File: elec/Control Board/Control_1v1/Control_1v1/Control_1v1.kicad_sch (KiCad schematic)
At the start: 104 parts, among them J1 DB9_Female_MountingHoles, J10 Conn_02x12_Odd_Even, J11 Screw_Terminal_01x02, J14 Conn_01x10, J2 Conn_01x08, J25 Screw_Terminal_01x02, J26 Conn_01x10, J27 Conn_02x12_Odd_Even, J28 Screw_Terminal_01x02, J29 Conn_01x10, J3 Conn_01x08, J4 Conn_01x08, J5 Conn_01x08, J6 Conn_01x08, J7 Conn_01x10, J8 Conn_02x18_Odd_Even, J9 Conn_01x10

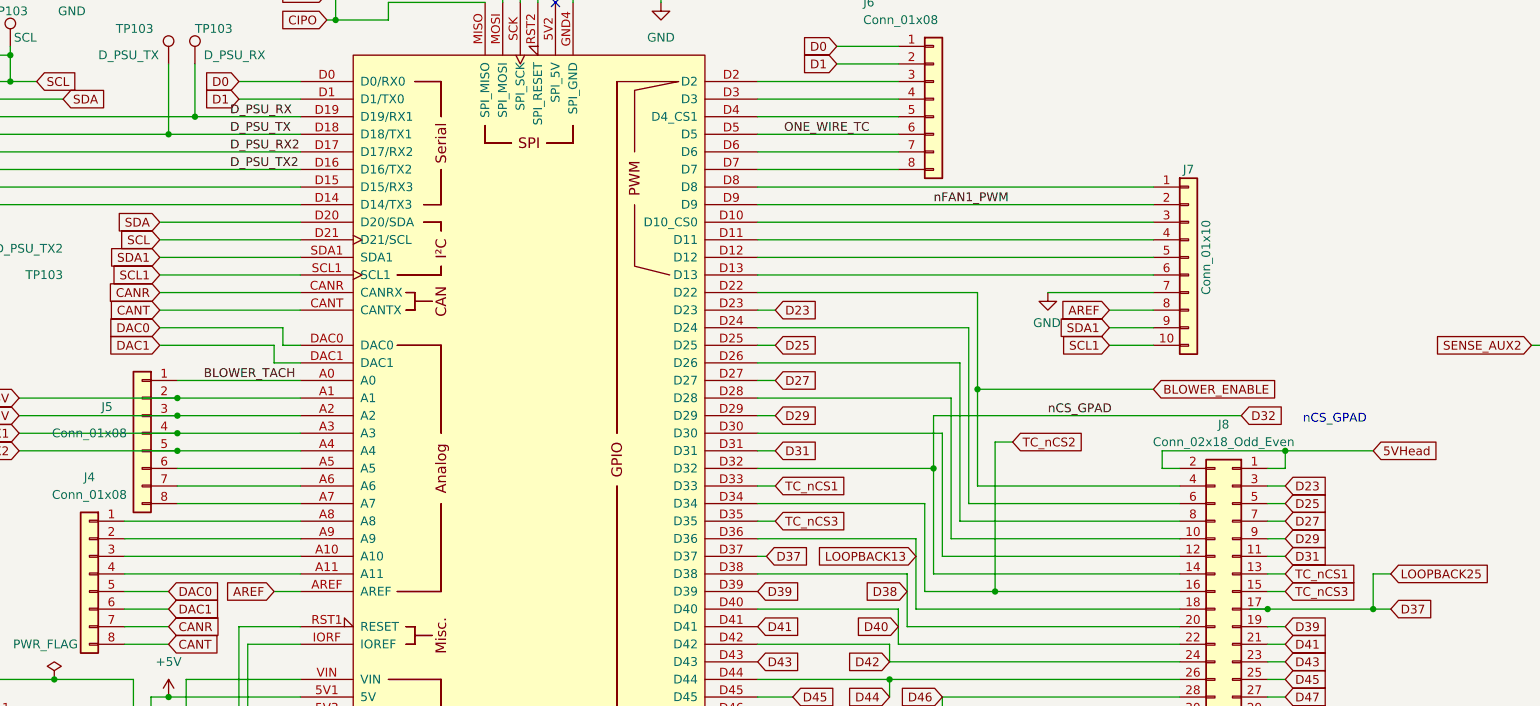
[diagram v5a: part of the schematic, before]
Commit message: Add LED_BUILTIN
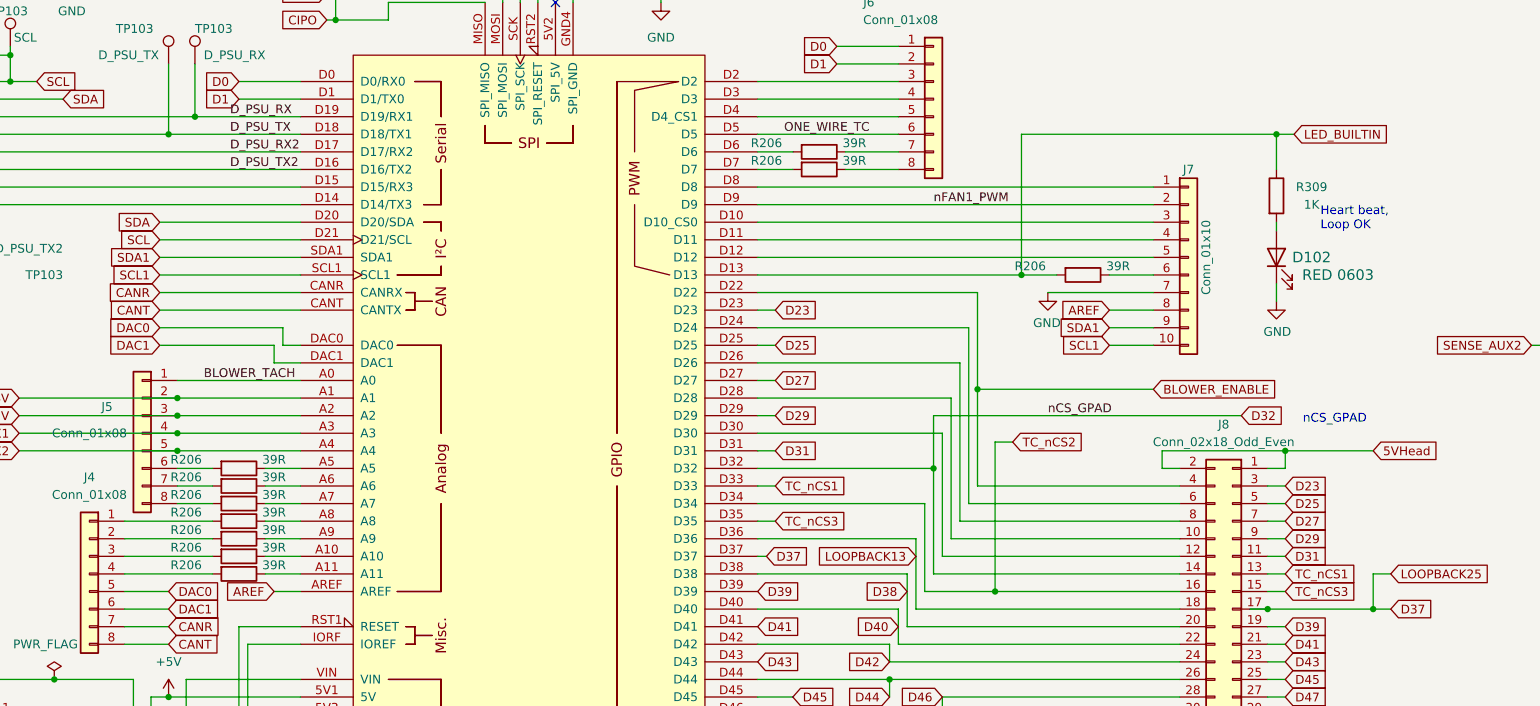
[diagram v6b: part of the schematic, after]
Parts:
- added D102: RED 0603, LED_SMD:LED_0603_1608Metric_Pad1.05x0.95mm_HandSolder, symbol Device:LED
- added R206 (x10): 39R, Resistor_SMD:R_0603_1608Metric_Pad0.98x0.95mm_HandSolder, symbol Device:R
- added R309: 1K, Resistor_SMD:R_0603_1608Metric_Pad0.98x0.95mm_HandSolder, symbol Device:R
- A1: footprint Arduino:Arduino_Due_Shield -> PubInv_KiCad_PCB:Arduino_Due_Shield_Annotated
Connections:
- net GND: now also D102.1 (K)
- net at A1.A10: now also R206.1; no longer J4.3 (Pin_3)
- net at A1.A11: now also R206.1; no longer J4.4 (Pin_4)
- net at A1.A5: now also R206.1; no longer J5.6 (Pin_6)
- net at A1.A6: now also R206.1; no longer J5.7 (Pin_7)
- net at A1.A7: now also R206.1; no longer J5.8 (Pin_8)
- net at A1.A8: now also R206.1; no longer J4.1 (Pin_1)
- net at A1.A9: now also R206.1; no longer J4.2 (Pin_2)
- net at J7.6 (Pin_6): now also R206.1; no longer A1.D13
- net at A1.D6: now also R206.2; no longer J6.7 (Pin_7)
- net at J6.8 (Pin_8): now also R206.1; no longer A1.D7
- new net: A1.D7, R206.2
- new net: D102.2 (A), R309.2
- new net: J4.1 (Pin_1), R206.2
- new net: J4.2 (Pin_2), R206.2
- new net: J4.3 (Pin_3), R206.2
- new net: J4.4 (Pin_4), R206.2
- new net: J5.7 (Pin_7), R206.2
- new net: J5.6 (Pin_6), R206.2
- new net: J5.8 (Pin_8), R206.2
- new net: J6.7 (Pin_7), R206.1
- new net LED_BUILTIN: A1.D13, R206.2, R309.1
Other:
- note added: "Heart beat, Loop OK"

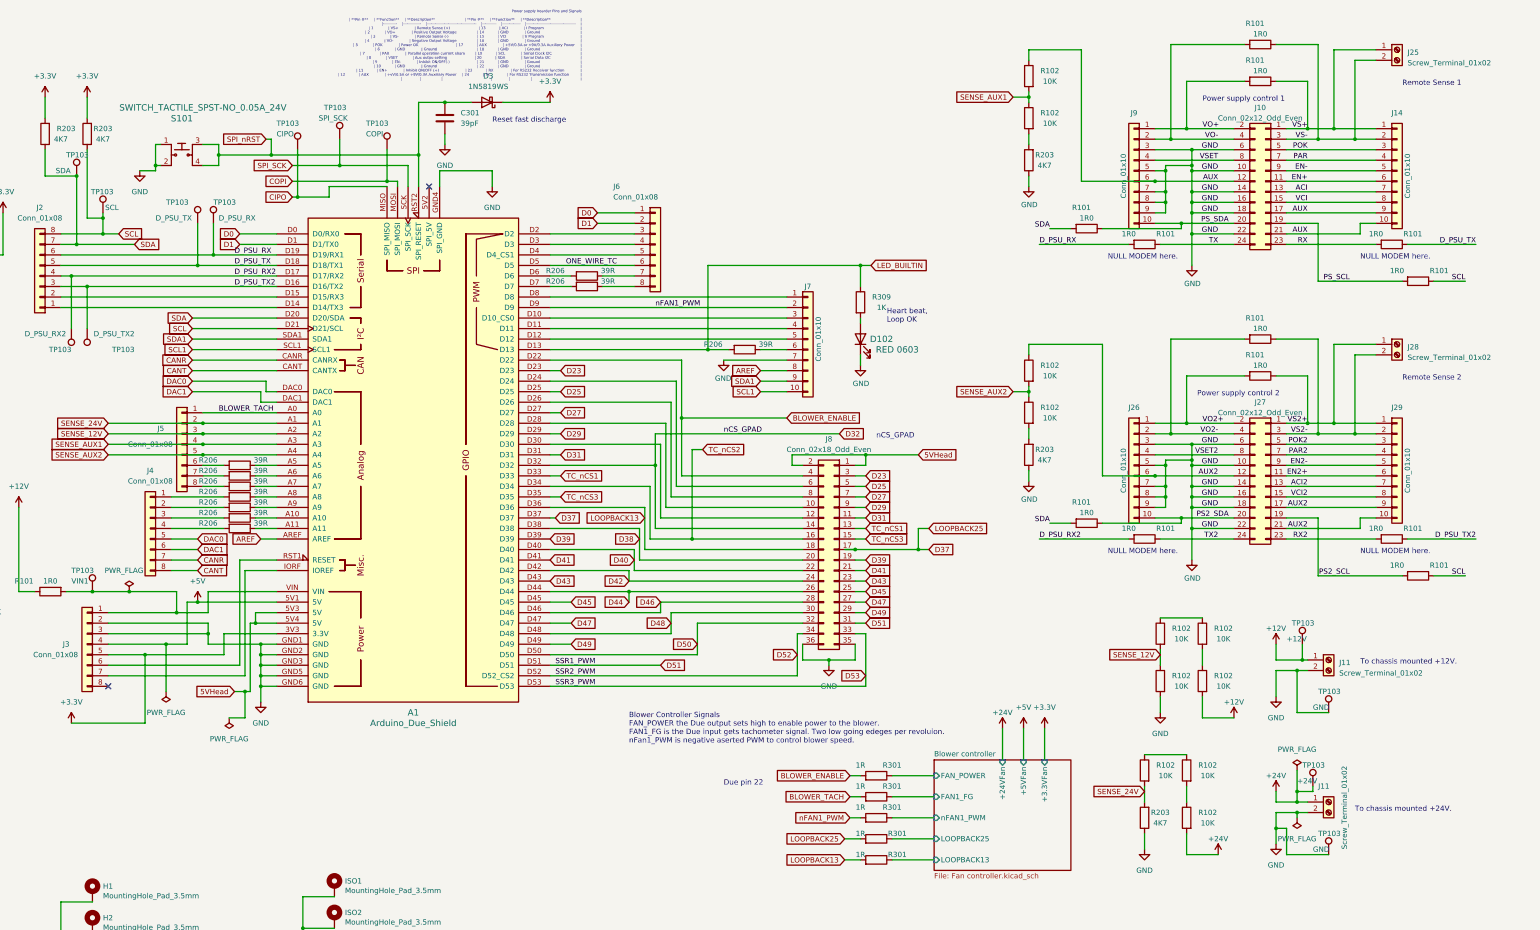
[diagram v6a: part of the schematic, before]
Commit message: Add power supply enable circuits. Add shutdown button.
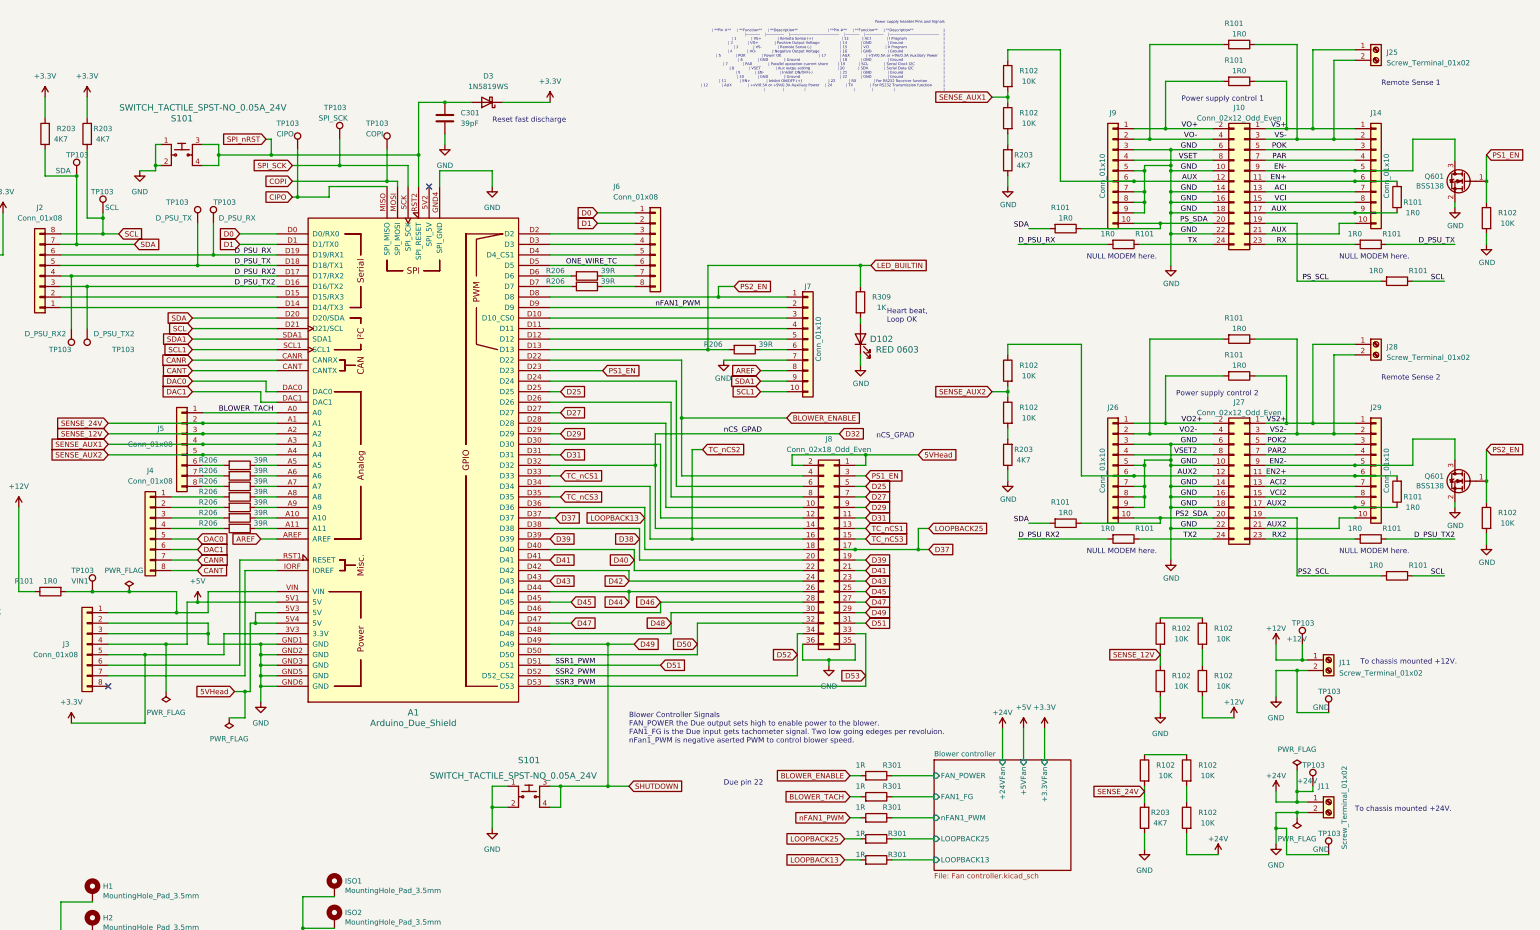
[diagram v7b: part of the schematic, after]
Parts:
- added Q601 (x2): BSS138, Package_TO_SOT_SMD:SOT-23, symbol Transistor_FET:BSS138
- added R101 (x2): 1R0, Resistor_SMD:R_0603_1608Metric_Pad0.98x0.95mm_HandSolder, symbol Device:R
- added R102 (x2): 10K, Resistor_SMD:R_0603_1608Metric_Pad0.98x0.95mm_HandSolder, symbol Device:R
- added S101: SWITCH_TACTILE_SPST-NO_0.05A_24V, PubInv_KiCad_PCB:Switch_Tactile_THT_6x6mm, symbol GPAD_SCH_LIB:SWITCH_TACTILE_SPST-NO_0.05A_24V
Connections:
- net AUX: now also R101.1
- net AUX2: now also R101.1
- net D49: now also S101.3, S101.4
- net EN+: now also R101.2
- net EN-: now also Q601.3 (D)
- net EN2+: now also R101.2
- net EN2-: now also Q601.3 (D)
- net GND: now also Q601.2 (S), Q601.2 (S), R102.2, R102.2, S101.1, S101.2
- net PS2_EN: now reaches A1.D8, J7.1 (Pin_1)
- net PS2_EN: now also Q601.1 (G), R102.1
- net D23 renamed PS1_EN
- net PS1_EN: now also Q601.1 (G), R102.1
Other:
- moved on the sheet: J10, J14, J25, J26, J27, J28, J29, J9, R101, R102, R203

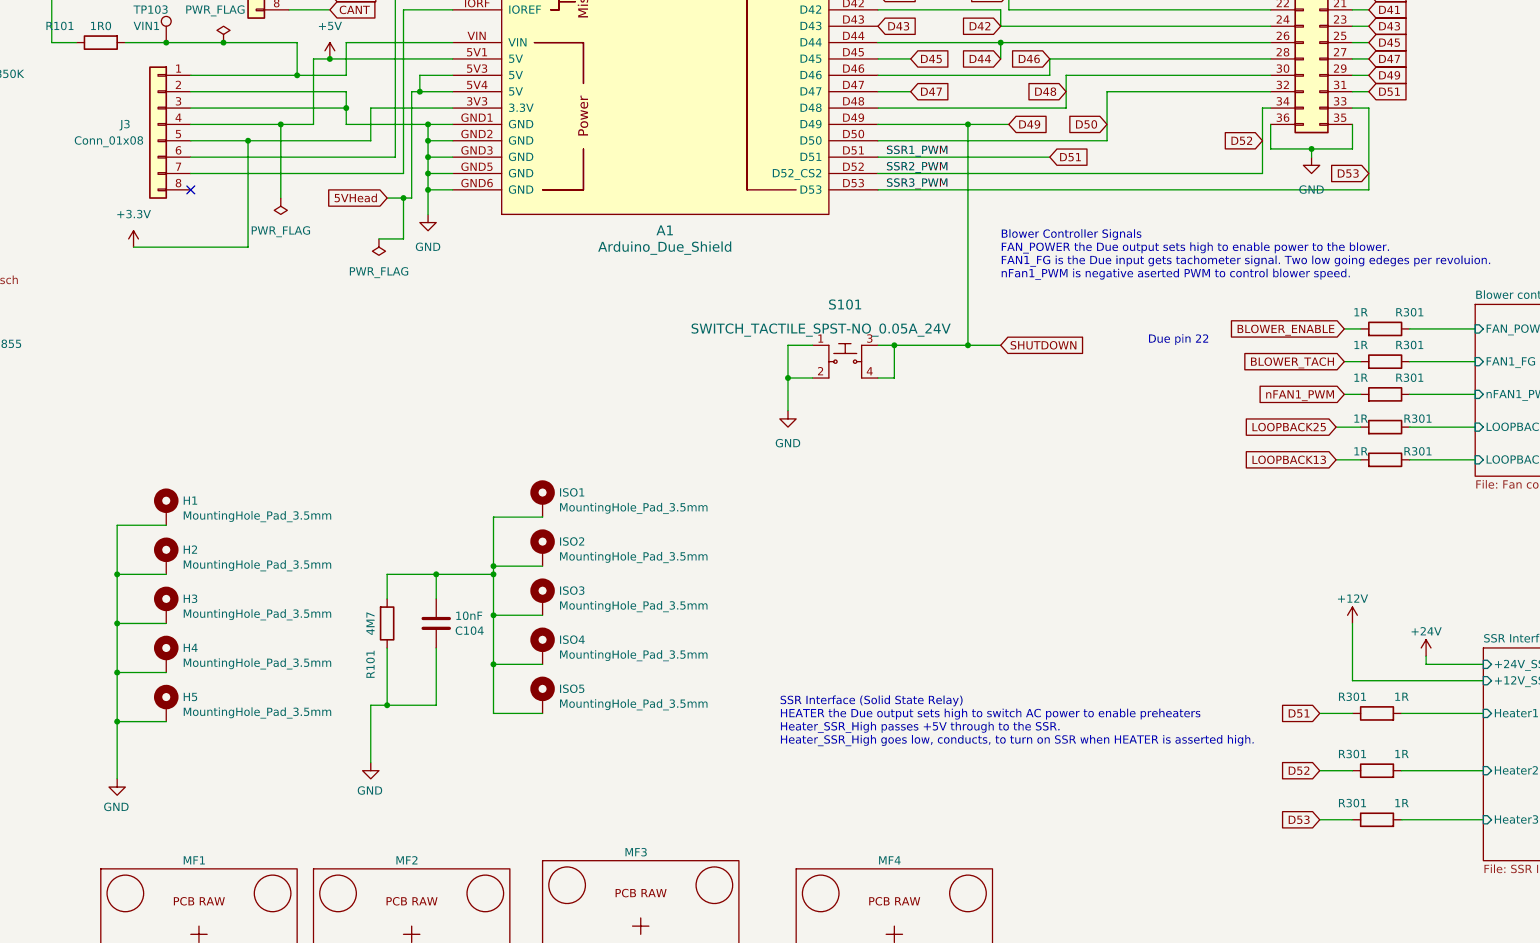
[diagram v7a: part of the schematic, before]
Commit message: Add power shutdown button. Add thermocouple ground screw terminals. Isolate SCL from SDA traces. Make first cut BOM.
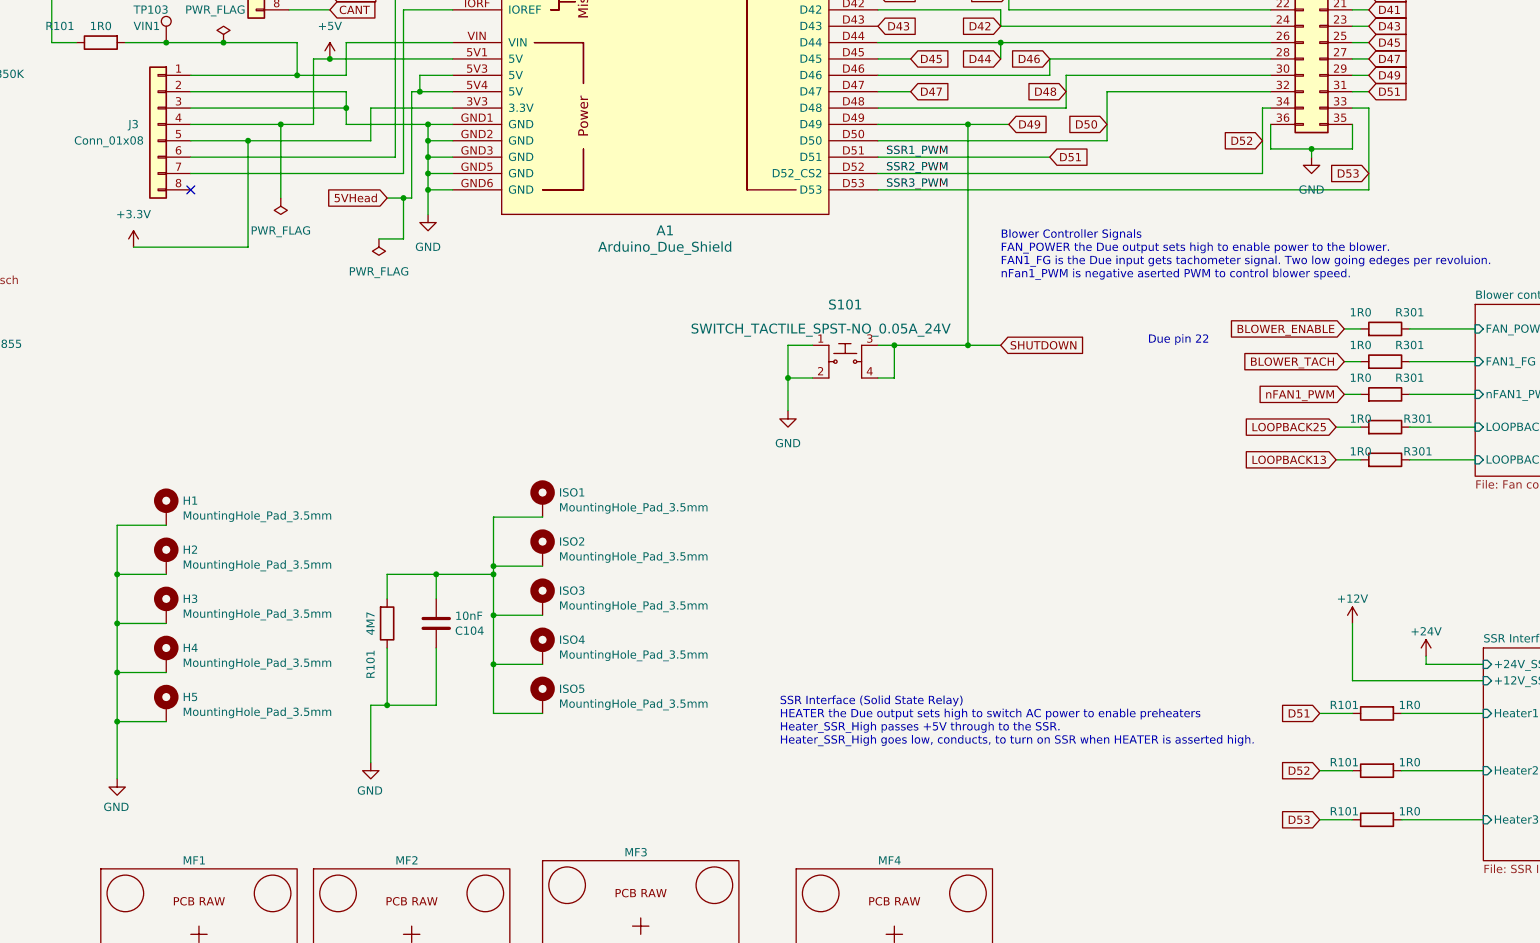
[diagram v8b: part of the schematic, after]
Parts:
- removed R301 (x3): 1R, Resistor_SMD:R_0603_1608Metric_Pad0.98x0.95mm_HandSolder, symbol Device:R
- added R101 (x3): 1R0, Resistor_SMD:R_0603_1608Metric_Pad0.98x0.95mm_HandSolder, symbol Device:R
- J3: footprint Connector_PinHeader_2.54mm:PinHeader_1x08_P2.54mm_Vertical -> Connector_PinSocket_2.54mm:PinSocket_1x08_P2.54mm_Vertical
- R101: LongLead (none) -> NO
- R301: value 1R -> 1R0; Distributor 1 NA -> JLCPCB; Distributor 1 PN NA -> C269434; MPN (none) -> RMC060315%N; Manufacturer (none) -> TyoHM
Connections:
- net D51: now also R101.1
- net D52: now also R101.1
- net D53: now also R101.1
- net SSR Interface/Heater1: now also R101.2
- net SSR Interface/Heater2: now also R101.2
- net SSR Interface/Heater3: now also R101.2
